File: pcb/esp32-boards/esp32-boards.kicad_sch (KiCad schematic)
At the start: 47 parts, among them J2 USB_B_Micro, J3 BATTERY, J4 LCD, Q1 Q_Photo_NPN, SW1 RESET, SW2 BATTERY_EN, SW3 START, SW4 BOOT_MODE, U1 ESP32-C3-WROOM-02, U2 MAX40200AUK, U3 MCP73831-2-OT, U4 LD39150DT33

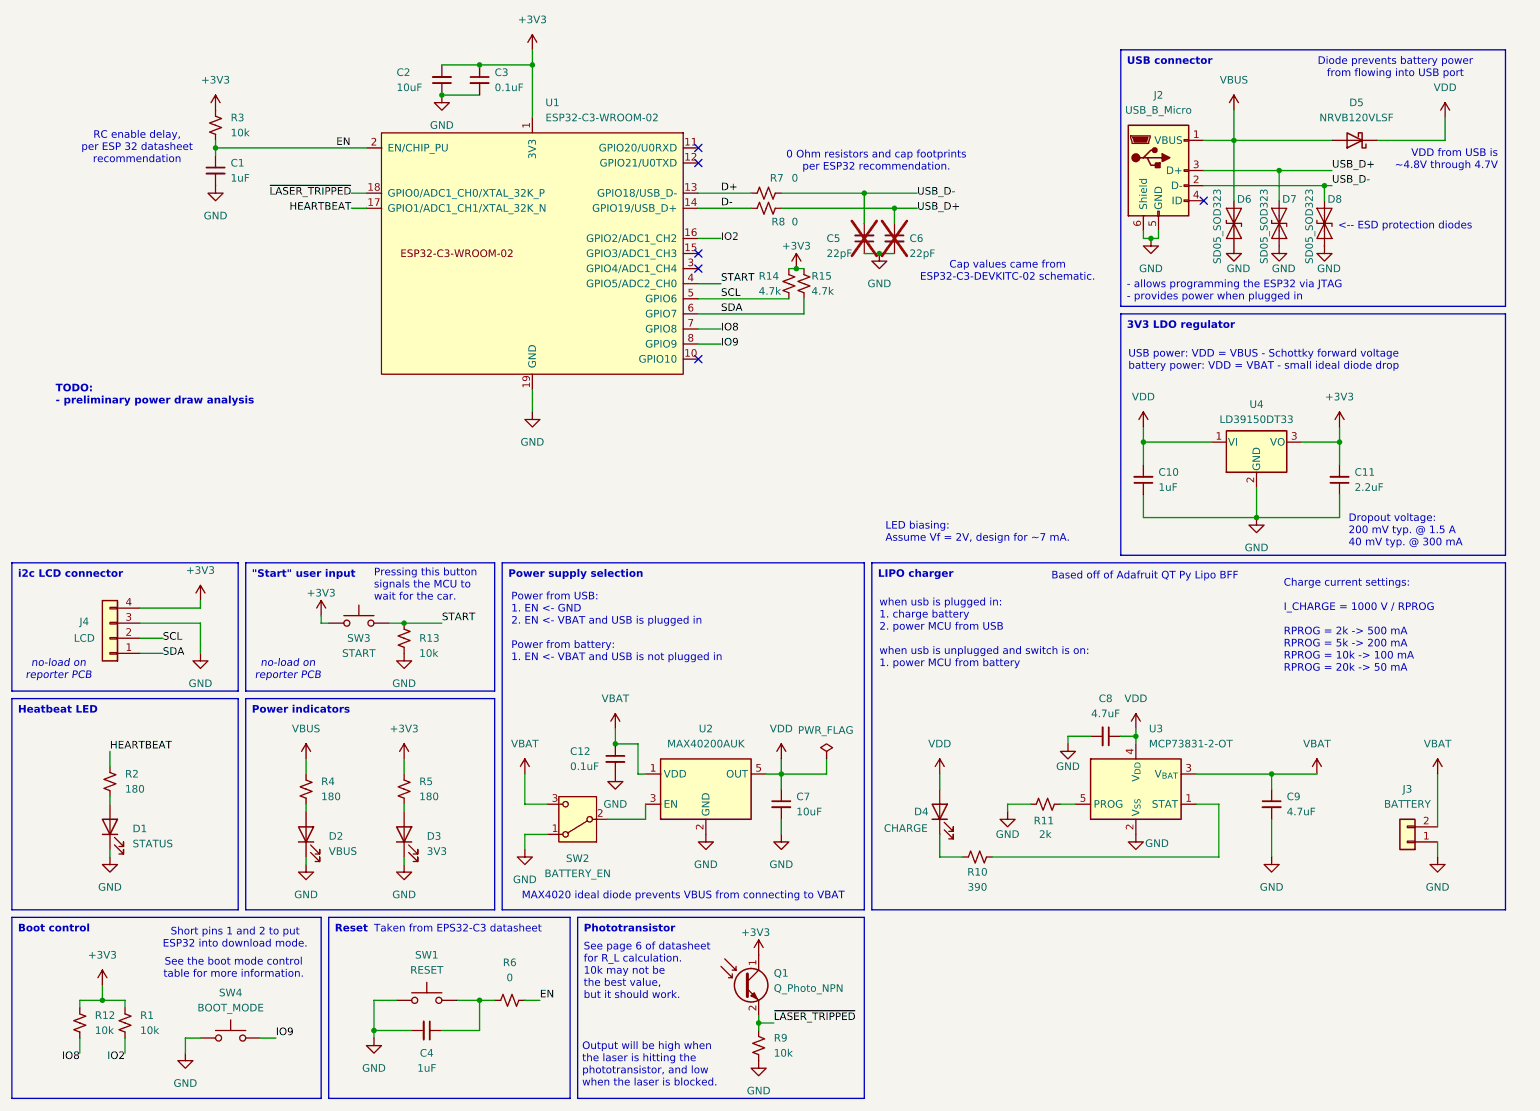
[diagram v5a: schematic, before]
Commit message: update reference designators
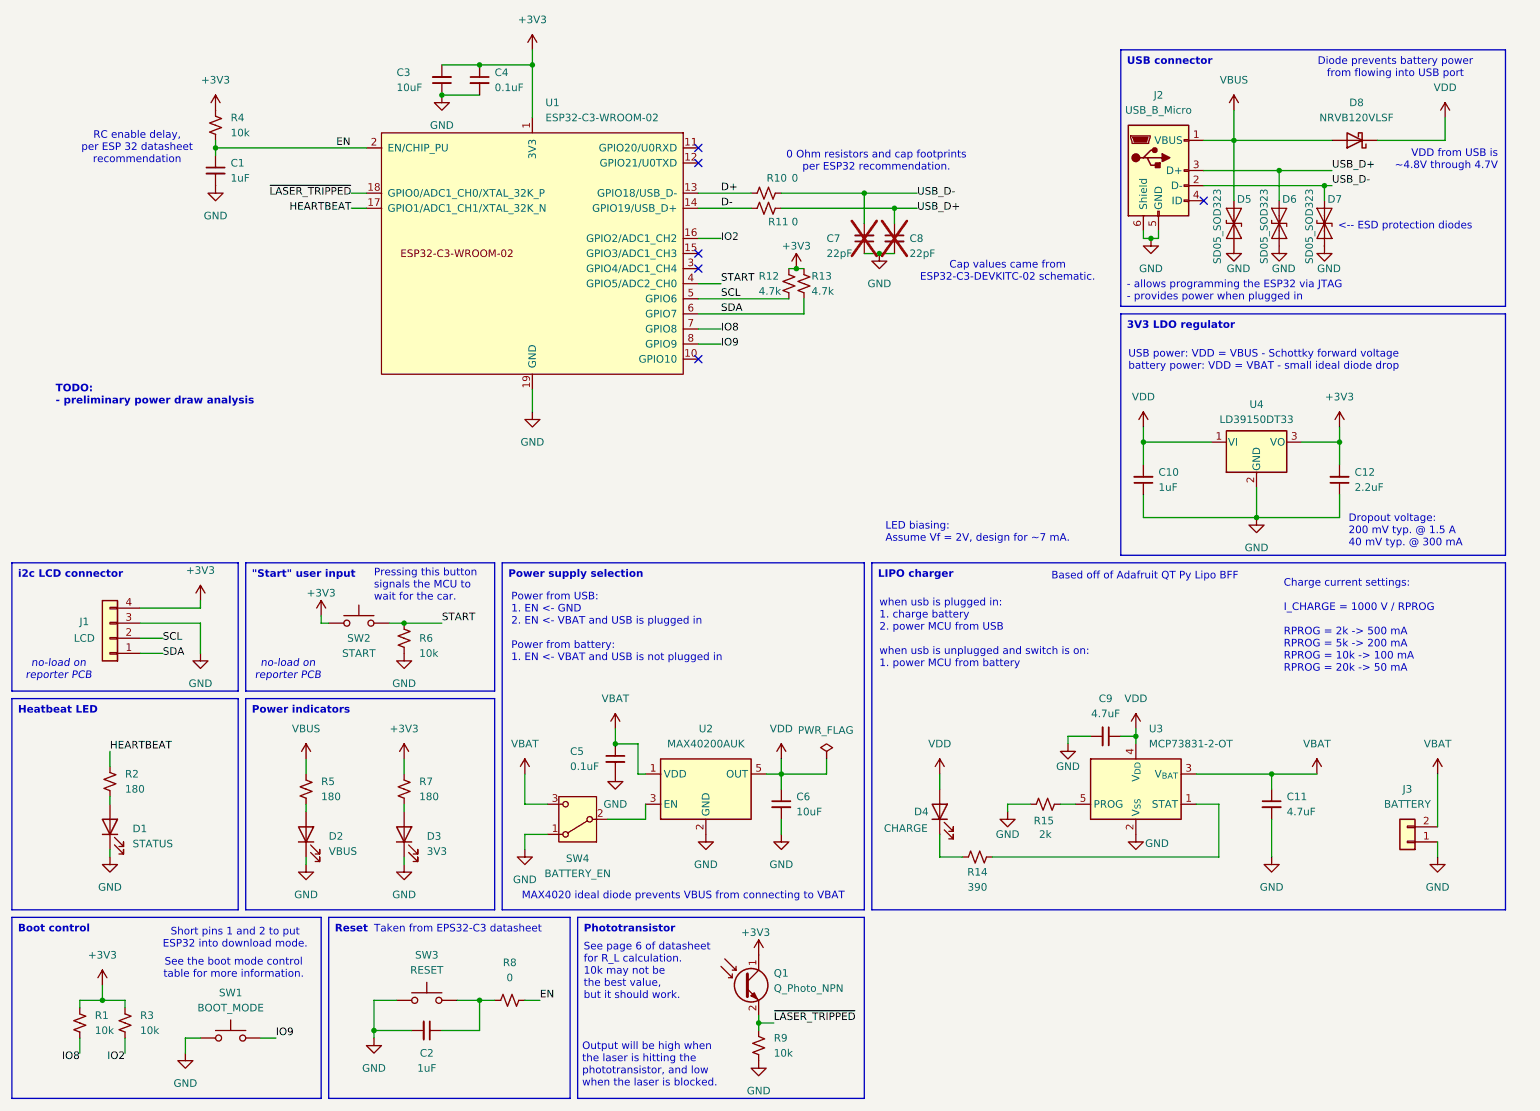
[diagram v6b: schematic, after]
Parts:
- renumbered C9 to C11, C11 to C12, C4 to C2, C2 to C3, C3 to C4, C12 to C5, C7 to C6, C5 to C7, C6 to C8, C8 to C9, D6 to D5, D7 to D6, D8 to D7, D5 to D8, J4 to J1, R12 to R1, R7 to R10, R8 to R11, R14 to R12, R15 to R13, R10 to R14, R11 to R15, R1 to R3, R3 to R4, R4 to R5, R13 to R6, R5 to R7, R6 to R8, SW4 to SW1, SW3 to SW2, SW1 to SW3, SW2 to SW4

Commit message: update BOMs for JLC assembly
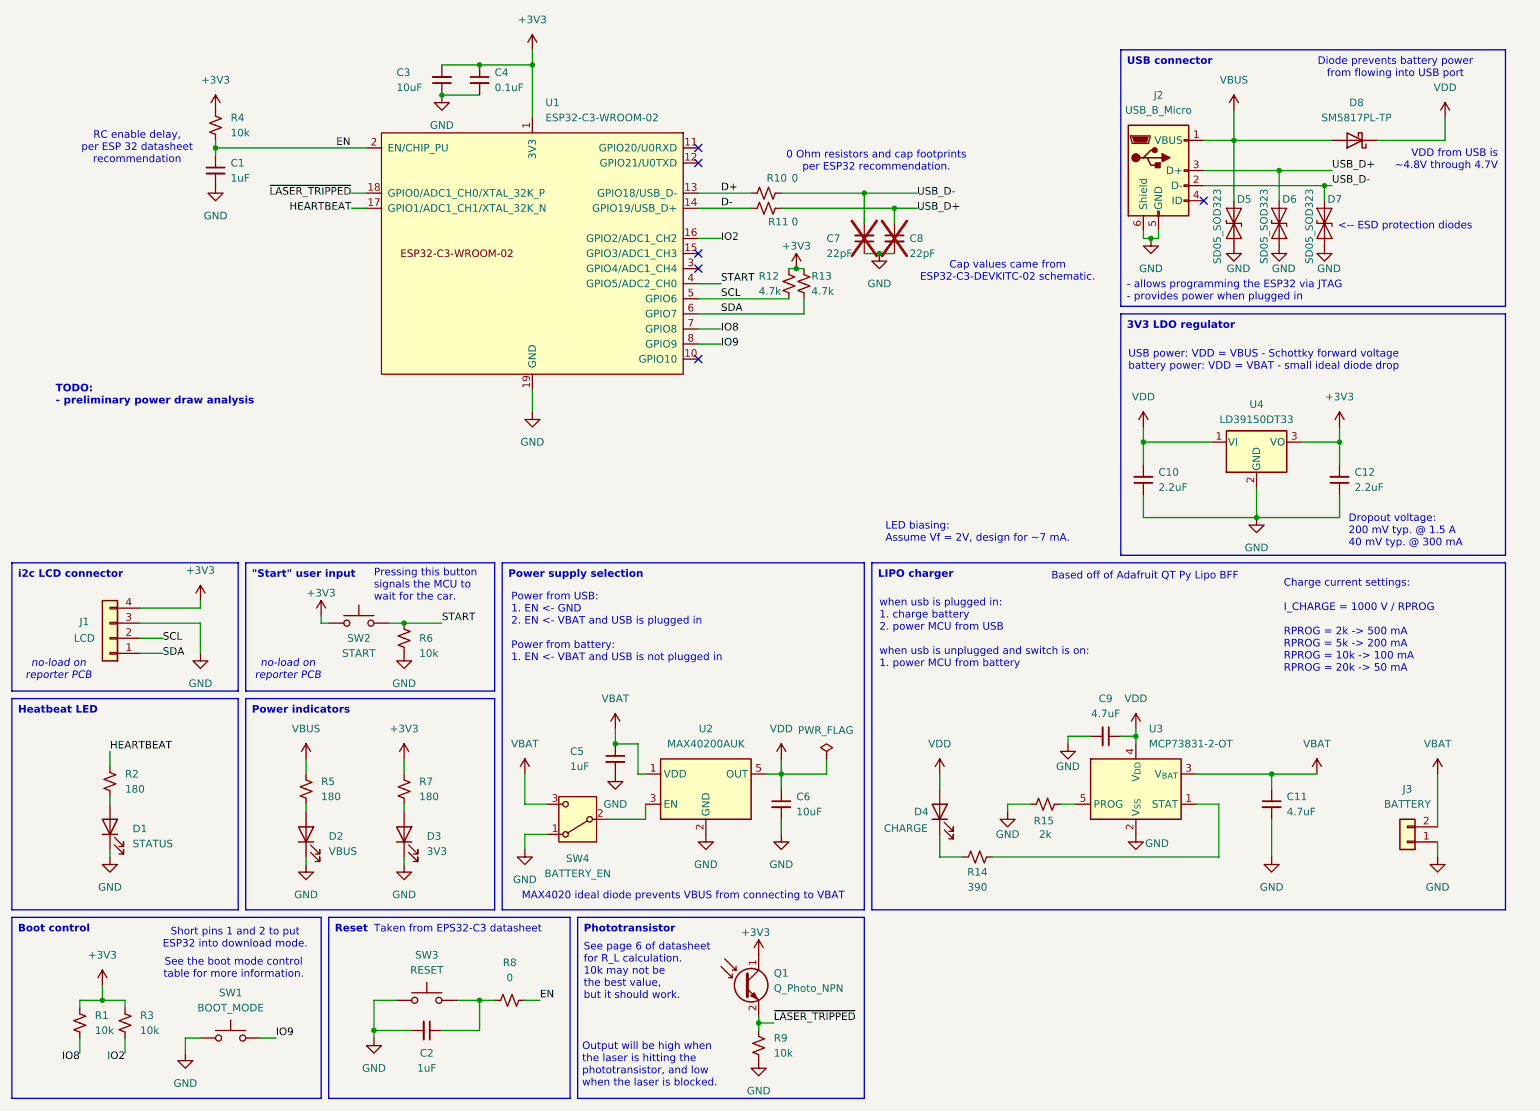
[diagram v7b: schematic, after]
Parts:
- C1, C2: JLC Part Number (none) -> C28323; Part Number (none) -> CC0805KFX7R6BB106
- C10: value 1uF -> 2.2uF; JLC Part Number (none) -> C377773; Part Number (none) -> CC0805KKX7R6BB225
- C11, C9: JLC Part Number (none) -> C1779; Part Number (none) -> CC0805KKX7R6BB475
- C12: JLC Part Number (none) -> C377773; Part Number (none) -> CC0805KKX7R6BB225
- C3, C6: JLC Part Number (none) -> C15850; Part Number (none) -> CC0805KKX7R6BB105
- C4: JLC Part Number (none) -> C49678; Part Number (none) -> CC0805KRX7R6BB104
- C5: value 0.1uF -> 1uF; JLC Part Number (none) -> C28323; Part Number (none) -> CC0805KFX7R6BB106
- C7, C8: JLC Part Number (none) -> C1804; Part Number (none) -> CC0805JRNPO9BN220
- D1, D2, D3, D4: JLC Part Number (none) -> C434438
- D5, D6, D7: JLC Part Number (none) -> C490614; Part Number SD05C-7 -> Leiditech SD05
- D8: value NRVB120VLSF -> SM5817PL-TP; JLC Part Number (none) -> C669022; Part Number NRVB120VLSF -> SM5817PL-TP
- J1: JLC Part Number (none) -> C131334
- J3, SW2: JLC Part Number (none) -> C5251182
- Q1: JLC Part Number (none) -> C2936540
- R1, R3, R4, R6, R9: JLC Part Number (none) -> C17414; Part Number (none) -> RC0805FR-0710KL
- R10, R11, R8: JLC Part Number (none) -> C17477; Part Number (none) -> RC0805JR-070RL
- R12, R13: JLC Part Number (none) -> C17673; Part Number (none) -> RC0805FR-074K7L
- R14: JLC Part Number (none) -> C17655; Part Number (none) -> RC0805FR-07390RL
- R15: JLC Part Number (none) -> C17604; Part Number (none) -> RC0805FR-072KL
- R2, R5, R7: JLC Part Number (none) -> C25270; Part Number (none) -> RC0805FR-07180RL
- SW4: JLC Part Number (none) -> C273395
- U1: JLC Part Number (none) -> C2934560
- U2: JLC Part Number (none) -> C2649430
- U3: JLC Part Number (none) -> C424093
- U4: JLC Part Number (none) -> C155559

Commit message: remove tooling holes; finalize for production
It's easier to have JLC add the tooling holes.
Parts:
- C1, C2, C5: JLC (none) -> 0805; JLC Part Number C28323 -> (none); JLCSC (none) -> C28323
- C10, C12: JLC (none) -> 0805; JLC Part Number C377773 -> (none); JLCSC (none) -> C377773
- C11, C9: JLC (none) -> 0805; JLC Part Number C1779 -> (none); JLCSC (none) -> C1779
- C3, C6: JLC (none) -> 0805; JLC Part Number C15850 -> (none); JLCSC (none) -> C15850
- C4: JLC (none) -> 0805; JLC Part Number C49678 -> (none); JLCSC (none) -> C49678
- C7, C8: JLC (none) -> 0805; JLC Part Number C1804 -> (none); JLCSC (none) -> C1804
- D1, D2, D3, D4: JLC (none) -> 1206; JLC Part Number C434438 -> (none); JLCSC (none) -> C434438
- D5, D6, D7: JLC (none) -> SD-323; JLC Part Number C490614 -> (none); JLCSC (none) -> C490614
- D8: JLC (none) -> SOD-123FL; JLC Part Number C669022 -> (none); JLCSC (none) -> C669022
- J1: JLC Part Number C131334 -> (none); JLCSC (none) -> C131334
- J3, SW2: JLC Part Number C5251182 -> (none); JLCSC (none) -> C5251182
- Q1: JLC Part Number C2936540 -> (none); JLCSC (none) -> C2936540
- R1, R3, R4, R6, R9: JLC (none) -> 0805; JLC Part Number C17414 -> (none); JLCSC (none) -> C17414
- R10, R11, R8: JLC (none) -> 0805; JLC Part Number C17477 -> (none); JLCSC (none) -> C17477
- R12, R13: JLC (none) -> 0805; JLC Part Number C17673 -> (none); JLCSC (none) -> C17673
- R14: JLC (none) -> 0805; JLC Part Number C17655 -> (none); JLCSC (none) -> C17655
- R15: JLC (none) -> 0805; JLC Part Number C17604 -> (none); JLCSC (none) -> C17604
- R2, R5, R7: JLC (none) -> 0805; JLC Part Number C25270 -> (none); JLCSC (none) -> C25270
- SW4: JLC Part Number C273395 -> (none); JLCSC (none) -> C273395
- U1: JLC (none) -> VFQFN-32-EP; JLC Part Number C2934560 -> (none); JLCSC (none) -> C2934560
- U2: JLC (none) -> SOT-23-5; JLC Part Number C2649430 -> (none); JLCSC (none) -> C2649430
- U3: JLC (none) -> SOT-23-5; JLC Part Number C424093 -> (none); JLCSC (none) -> C424093
- U4: JLC (none) -> TO-252; JLC Part Number C155559 -> (none); JLCSC (none) -> C155559
